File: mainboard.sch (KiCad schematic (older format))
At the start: 44 parts, among them J1 Screw_Terminal_1x02, SW1 SW_Push, SW2 SW_Push, U1 AT90CAN128-16MU, U2 MCP2551-I/SN, Y1 Crystal

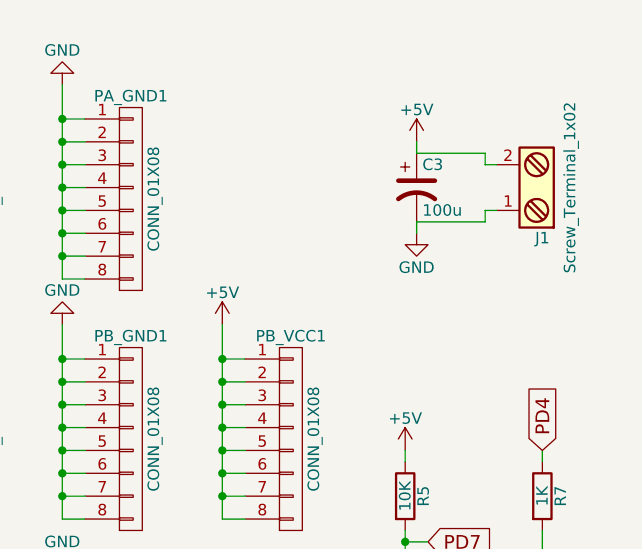
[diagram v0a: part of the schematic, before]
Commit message: Added new smd components, still need protection circuit and routing
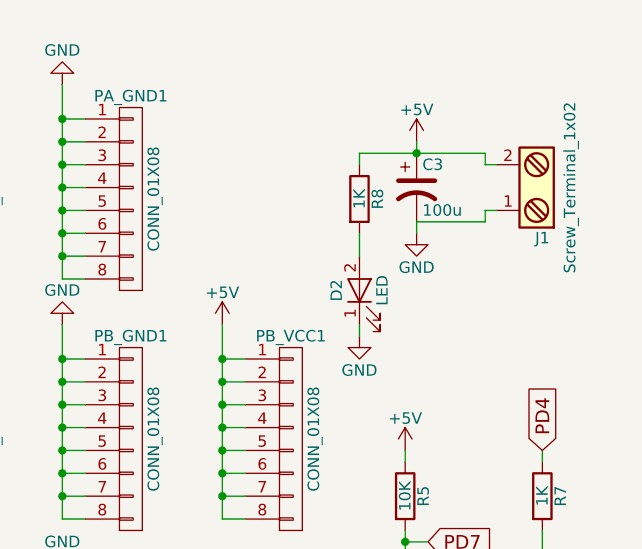
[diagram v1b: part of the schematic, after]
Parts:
- added D2: LED, LEDs:LED_1206, symbol LED
- added R8: 1K, Resistors_SMD:R_1206, symbol R
- C3, C4, C5: footprint Capacitors_THT:CP_Radial_D6.3mm_P2.50mm -> Capacitors_SMD:CP_Elec_6.3x4.5
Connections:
- net +5V: now also R8.1
- net GND: now also D2.1 (K)
- new net: D2.2 (A), R8.2

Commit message: Added protection, made board design and routing
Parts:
- removed PE_GND1: CONN_01X06, Pin_Headers:Pin_Header_Straight_1x06_Pitch2.00mm, symbol CONN_01X06
- added C10: 100u, Capacitors_THT:CP_Radial_D7.5mm_P2.50mm, symbol CP1
- added C11, C9: 100u, Capacitors_THT:CP_Radial_D7.5mm_P2.50mm, symbol CP
- added Q1: IRF9540N, TO_SOT_Packages_SMD:TO-252-2, symbol IRF9540N
- added SENSOR1: CONN_01X06, Pin_Headers:Pin_Header_Straight_1x06_Pitch2.54mm, symbol CONN_01X06
- added SW_SMD1: RESET_SW, Buttons_Switches_SMD:SW_DIP_x1_W7.62mm_Slide_Copal_CHS-B, symbol SW_Push
- added SW_SMD2: DEBUG_SW, Buttons_Switches_SMD:SW_DIP_x1_W7.62mm_Slide_Copal_CHS-B, symbol SW_Push
- added Y_SMD1: Crystal, Crystals:Crystal_SMD_HC49-SD, symbol Crystal
- C1, C2: footprint Capacitors_SMD:C_1210 -> Capacitors_SMD:C_1206
- CAN1, CAN2, CAN4, I2C1, UART0, UART1: footprint Pin_Headers:Pin_Header_Straight_1x04_Pitch2.00mm -> Pin_Headers:Pin_Header_Straight_1x04_Pitch2.54mm
- PA1, PA_GND1, PB1, PB_GND1, PB_VCC1, PC1, PC_GND1, PF1, PF_GND1: footprint Pin_Headers:Pin_Header_Straight_1x08_Pitch2.00mm -> Pin_Headers:Pin_Header_Straight_1x08_Pitch2.54mm
- PE1, PE_GND2, SPI1: footprint Pin_Headers:Pin_Header_Straight_1x06_Pitch2.00mm -> Pin_Headers:Pin_Header_Straight_1x06_Pitch2.54mm
- PG1, PG_GND1: footprint Pin_Headers:Pin_Header_Straight_1x05_Pitch2.00mm -> Pin_Headers:Pin_Header_Straight_1x05_Pitch2.54mm
- SERVO1: footprint Pin_Headers:Pin_Header_Straight_1x03_Pitch2.00mm -> Pin_Headers:Pin_Header_Straight_1x03_Pitch2.54mm
- SW_TH1: renamed from SW2; value SW_Push -> RESET_SW
- SW_TH2: renamed from SW1; value SW_Push -> DEBUG_SW
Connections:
- net +5V: now also C10.1, C9.1, Q1.3 (S); no longer J1.2
- net GND: now also C10.2, C11.2, C9.2, Q1.1 (G), SW_SMD1.2, SW_SMD2.2
- net PA0: now also SENSOR1.1 (P1)
- net PA1: now also SENSOR1.2 (P2)
- net PA2: now also SENSOR1.3 (P3)
- net PA3: now also SENSOR1.4 (P4)
- net PA4: now also SENSOR1.5 (P5)
- net PA5: now also SENSOR1.6 (P6)
- net PD7: now also SW_SMD2.1
- net RESET: now also C11.1, SW_SMD1.1
- net at C1.1, U1.23 (XTAL2), Y1.1: now also Y_SMD1.1
- net at C2.1, U1.24 (XTAL1), Y1.2: now also Y_SMD1.2
- new net: J1.2, Q1.2 (D)
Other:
- note added: "5V input\n\n"
- note added: "AT90CAN128\n"
- note added: "CAN transceiver pins\n\n"
- note added: "CAN transceiver\n"
- note added: "Debug LED and user input\n\n\n"
- note added: "Decoupling capacitors\n\n\n"
- note added: "I2C pinout\n\n\n"
- note added: "PORTA pinout\n\n\n"
- note added: "PORTB pinout\n\n\n"
- note added: "PORTC pinout\n\n\n"
- note added: "PORTE pinout\n\n\n"
- note added: "PORTF pinout\n\n\n"
- note added: "PORTG pinouts\n\n"
- note added: "PROGRAMMATOR pinout\n\n\n"
- note added: "RESET circuit\n\n\n"
- note added: "SENSOR CONNECTOR\n\n\n\n"
- note added: "SERVO pinout\n\n\n"
- note added: "SPI pinout\n\n\n"
- note added: "UART0 pinout\n\n\n"
- note added: "UART1 pinout\n\n\n"
- moved on the sheet: C1, C2, C3, C4, C5, C6, C7, C8, CAN1, CAN2, CAN4, D1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

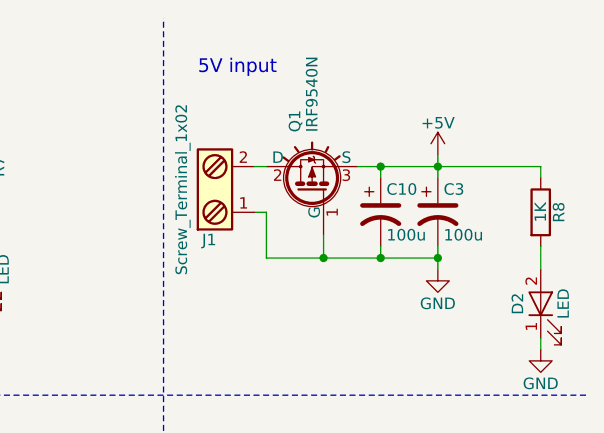
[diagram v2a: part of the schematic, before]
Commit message: Modified mosfet protection to smd
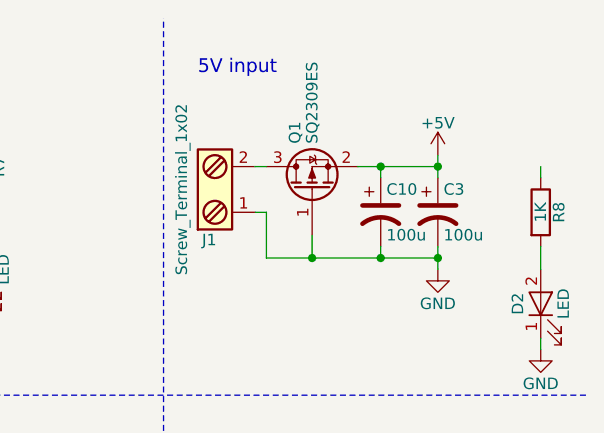
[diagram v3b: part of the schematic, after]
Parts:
- removed Q1: IRF9540N, TO_SOT_Packages_SMD:TO-252-2, symbol IRF9540N
- added Q1: SQ2309ES, TO_SOT_Packages_SMD:SOT-23, symbol BSS84
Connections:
- net +5V: now also Q1.2 (S); no longer R8.1
- net GND: now also Q1.1 (G)
- net at J1.2: now also Q1.3 (D)

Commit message: Did some power things
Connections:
- net +5V: now also R8.1
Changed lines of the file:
@@
 	14850 1400 14850 1500
 Connection ~ 14850 1500
+$Comp
+L +5V #PWR?
+U 1 1 59A68F6B
+P 15850 1100
+F 0 "#PWR?" H 15850 950 50  0001 C CNN
+F 1 "+5V" H 15850 1240 50  0000 C CNN
+F 2 "" H 15850 1100 50  0001 C CNN
+F 3 "" H 15850 1100 50  0001 C CNN
+	1    15850 1100
+	1    0    0    -1
+$EndComp
 $EndSCHEMATC

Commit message: New idea around servo power and new mosfet version for protection
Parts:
- removed SERVO1: CONN_01X03, Pin_Headers:Pin_Header_Straight_1x03_Pitch2.54mm, symbol CONN_01X03
- added C12: 100u, Capacitors_THT:CP_Radial_D7.5mm_P2.50mm, symbol CP1
- added C13: 100u, Capacitors_SMD:CP_Elec_6.3x4.5, symbol CP1
- added J2: SERVO 5V, Connectors_Terminal_Blocks:TerminalBlock_Pheonix_MPT-2.54mm_2pol, symbol Screw_Terminal_1x02
- added SERO_5V1, SERVO1, SERVO_GND1: CONN_01X04, Pin_Headers:Pin_Header_Straight_1x04_Pitch2.54mm, symbol CONN_01X04
- Q1: value SQ2309ES -> IRLR024NPBF; footprint TO_SOT_Packages_SMD:SOT-23 -> TO_SOT_Packages_SMD:TO-252-2
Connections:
- net +5V: now also J1.2, Q1.1 (G); no longer Q1.2 (S)
- net GND: now also Q1.3 (D), C12.2, C13.2, J2.1, SERVO_GND1.1 (P1), SERVO_GND1.2 (P2), SERVO_GND1.3 (P3), SERVO_GND1.4 (P4); no longer J1.1, Q1.1 (G)
- net PB7: now also SERVO1.4 (P4)
- net PE3: now also SERVO1.1 (P1)
- net PE4: now also SERVO1.2 (P2)
- net PE5: now also SERVO1.3 (P3)
- new net: J1.1, Q1.2 (S)
- new net +5C: C12.1, C13.1, J2.2, SERO_5V1.1 (P1), SERO_5V1.2 (P2), SERO_5V1.3 (P3), SERO_5V1.4 (P4)
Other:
- moved on the sheet: Q1
